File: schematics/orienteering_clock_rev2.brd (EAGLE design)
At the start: 100 x 80 mm, 53 parts, among them IC1 TPIC6B595N, IC2 TPIC6B595N, J2 ICSP, Q1 IRFU9024V, Q2 IRFU9024V, Q3 IRFU9024V, Q4 IRFU9024V, Q5 IRFU9024V, Q6 IRFU9024V, T1 BC547, Y2 16MHz

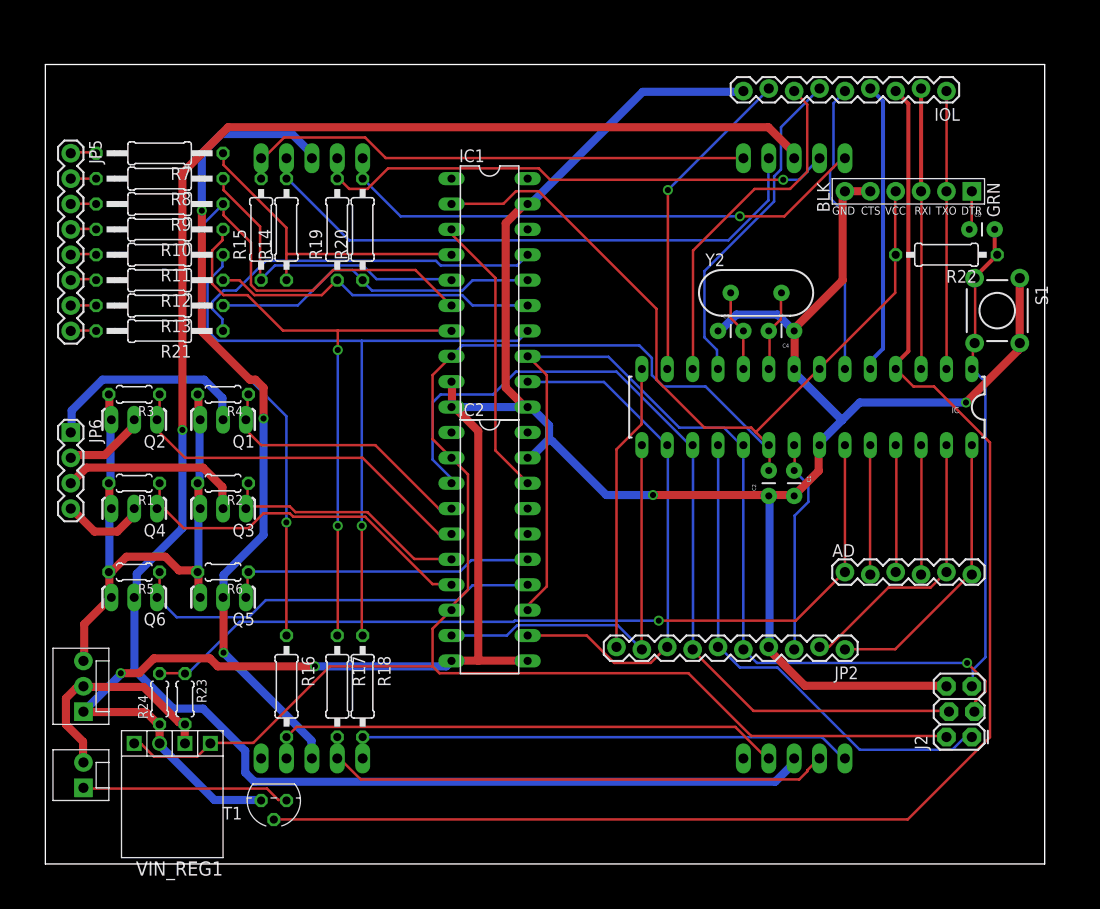
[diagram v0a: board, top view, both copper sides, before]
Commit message: schematics: improvements
- better packages for resistors
- slightly better placement
- added power_out outlet
- wider net for VCC
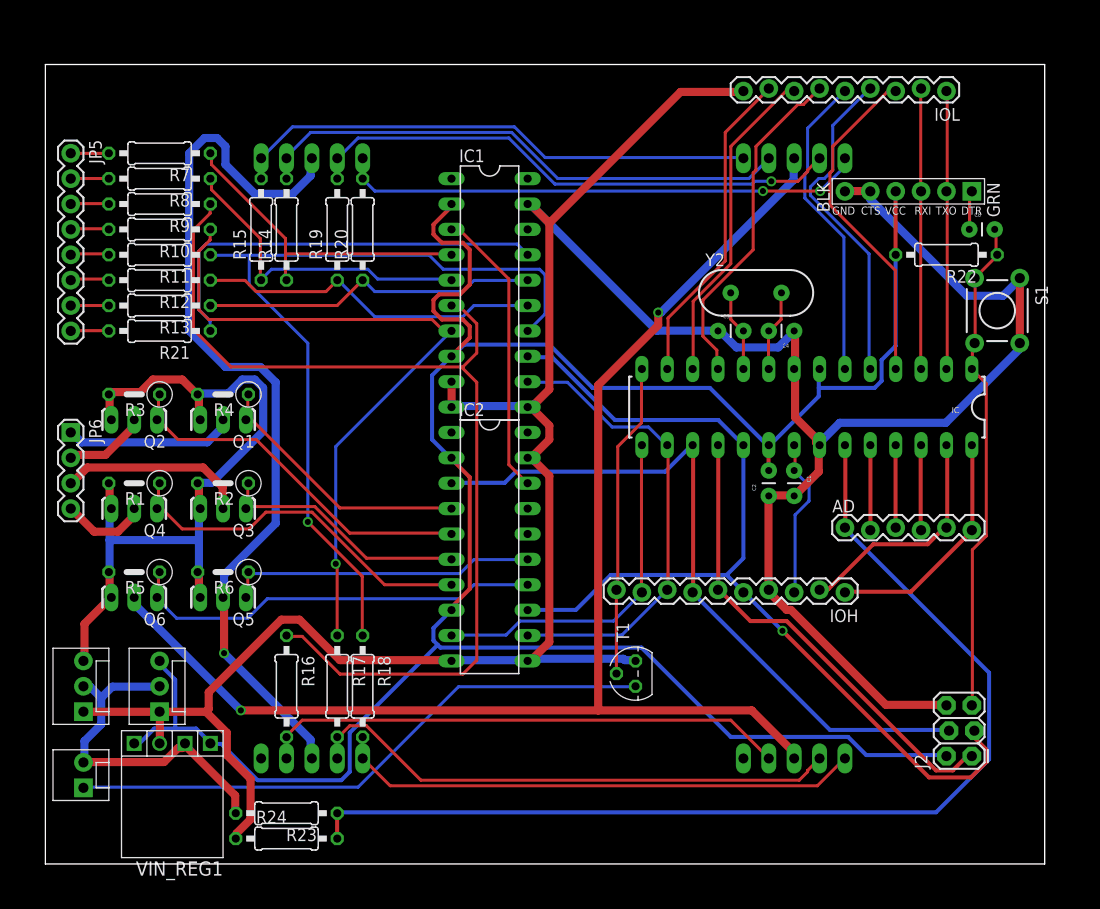
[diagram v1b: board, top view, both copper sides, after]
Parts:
- added IOH: M10LOCK, SparkFun-Connectors:1X10_LOCK
- JP2: value M10LOCK -> POWER_OUT; device SparkFun-Connectors:1X10_LOCK -> SparkFun-Connectors:MOLEX-1X3
- R1, R2, R3, R4, R5, R6: device resistor:0204/5 -> resistor:0207/5V
- R10, R11, R12, R13, R21, R7, R8, R9: device resistor:0207/12 -> resistor:0207/10
- R23, R24: device resistor:0204/5 -> resistor:0207/10
- moved JP2 68.9 mm to (11.4, 15.2), turned to 90 degrees
- moved T1 38.4 mm to (59.1, 19.1), turned to 90 degrees
- moved R24 18.9 mm to (24.1, 2.54), turned to 0 degrees
- moved R23 15.3 mm to (24.1, 5.08), turned to 180 degrees
- moved AD 4.45 mm to (80.0, 33.7)
- moved J2 1.90 mm to (92.7, 10.8)
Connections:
- net AD4/SDA: now also IOH.2; no longer JP2.2
- net AD5/SCL: now also IOH.1; no longer JP2.1
- net AREF: now also IOH.3; no longer JP2.3
- net GND: now also IOH.4, JP2.1; no longer JP2.4
- net IO2: no longer T1.2
- net IO8: now also IOH.10, T1.2; no longer JP2.10
- net IO9: now also IOH.9; no longer JP2.9
- net MISO: now also IOH.6; no longer JP2.6
- net MOSI: now also IOH.7; no longer JP2.7
- net SCK: now also IOH.5; no longer JP2.5
- net SS: now also IOH.8; no longer JP2.8
- net VCC: now also JP2.3
- net VIN: now also JP2.2
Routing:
- net IO2: track 145.9 -> 33.7 mm
- net A_S2: track 189.6 -> 136.9 mm, vias 1 -> 2
- net BUZZ_-: track 20.9 -> 59.4 mm
- net AD0: track 85.5 -> 107.5 mm, vias 1 -> 0
- net D2: track 79.3 -> 101.1 mm, vias 1 -> 0
- net DISP_12V: track 59.5 -> 76.1 mm
- net MOSI: track 88.0 -> 71.9 mm
- net VIN: track 23.0 -> 35.9 mm
- net D4: track 70.7 -> 83.4 mm
- net A_S1: track 81.9 -> 90.9 mm, vias 3 -> 1
- net D3: track 62.4 -> 70.0 mm, vias 2 -> 1
- net GND: track 301.6 -> 308.8 mm, vias 4 -> 0
- net SS: track 52.6 -> 47.0 mm
- net AREF: track 21.7 -> 16.1 mm
- net IO9: track 40.9 -> 35.7 mm
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
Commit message: schematics: redid connections to comply with various DRC
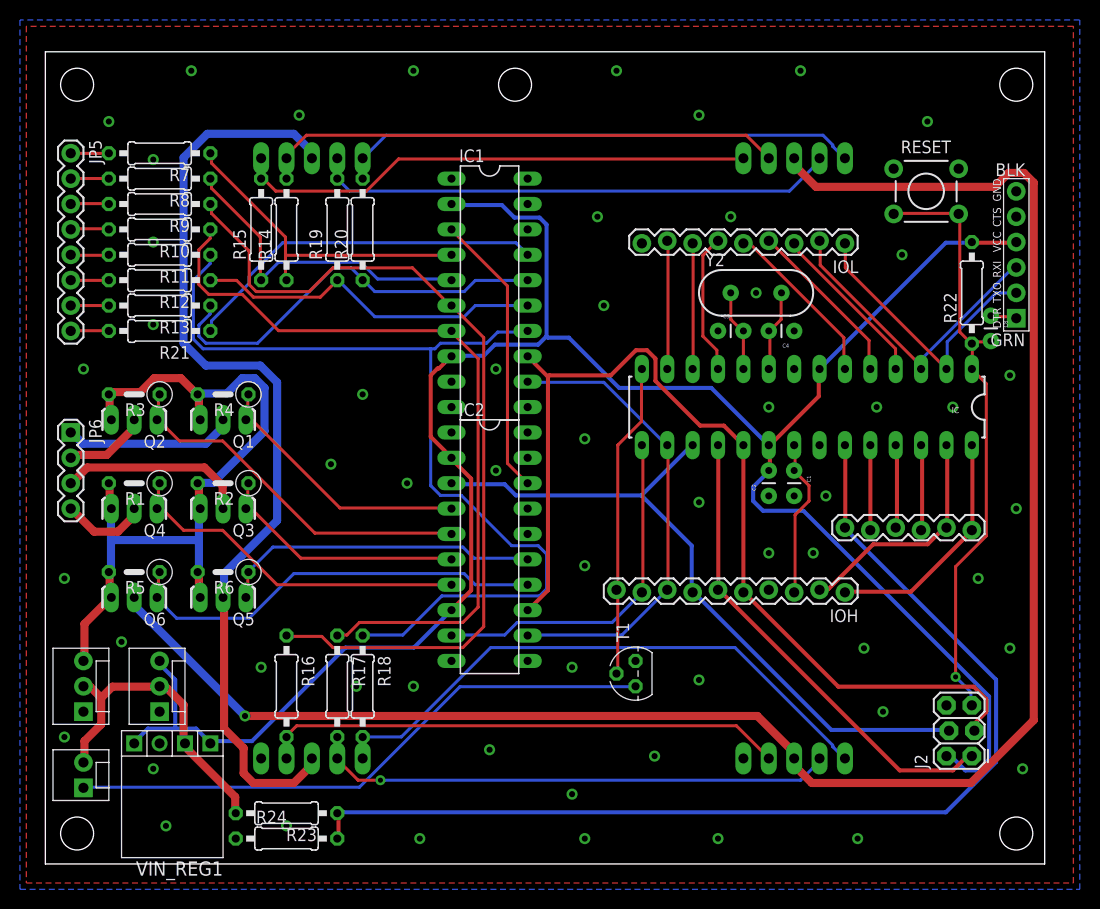
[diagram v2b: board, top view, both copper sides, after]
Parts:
- removed S1: RESET, SparkFun:TACTILE-PTH
- added JP10, JP11, JP4, JP8, JP9: STAND-OFF, SparkFun:STAND-OFF
- added RESET: RESET, SparkFun:TACTILE-PTH
- AD: value (none) -> AD
- moved IOL 18.3 mm to (80.0, 62.2)
- moved JP7 12.5 mm to (97.2, 61.0), turned to 90 degrees
- moved C8 8.90 mm to (94.6, 54.9), turned to 270 degrees
- moved R22 4.58 mm to (92.7, 57.1), turned to 90 degrees
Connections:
- net GND: now also RESET.1, RESET.2; no longer S1.1, S1.2
- net RESET: now also RESET.3, RESET.4; no longer S1.3, S1.4
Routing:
- net GND: track 308.8 -> 0.00 mm, vias 0 -> 56
- net A_S2: track 136.9 -> 181.8 mm, vias 2 -> 1
- net IO6: track 32.5 -> 12.6 mm
- net IO5: track 33.9 -> 14.1 mm
- net IO7: track 32.3 -> 12.9 mm
- net VCC: track 236.8 -> 218.2 mm
- net IO2: track 33.7 -> 16.8 mm
- net IO3: track 33.4 -> 17.1 mm
- net IO4: track 31.2 -> 17.2 mm
- net D2: track 101.1 -> 87.4 mm
- net D4: track 83.4 -> 95.7 mm, vias 1 -> 0
- net RESET: track 50.1 -> 61.0 mm, vias 0 -> 1
- net D6: track 33.7 -> 41.3 mm
- net D3: track 70.0 -> 77.2 mm, vias 1 -> 0
- net LS_E: track 52.7 -> 58.9 mm
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- added copper zone on layer 1, net GND
- added copper zone on layer 16, net GND
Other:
- board size 100 x 80 mm -> 100 x 81.3 mm

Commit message: schematics: part names smashing for silkscreen
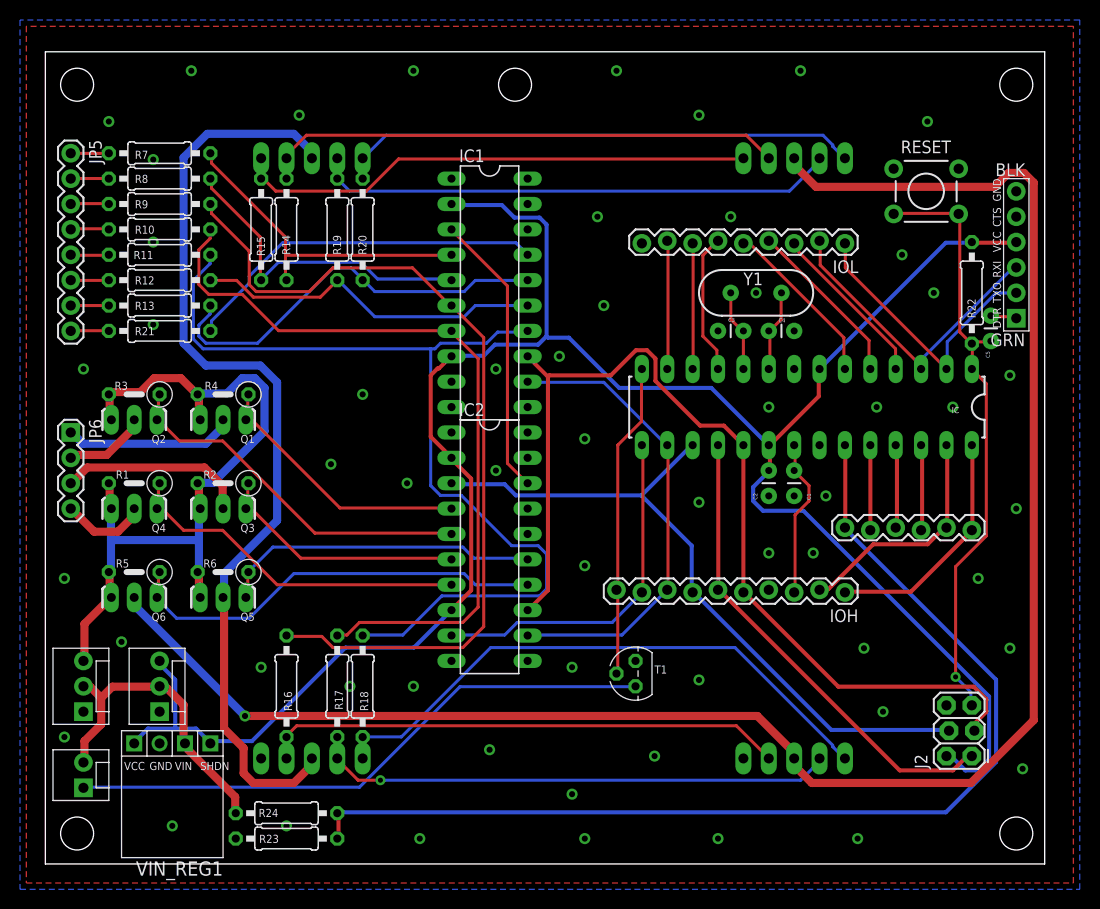
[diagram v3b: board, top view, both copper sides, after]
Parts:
- R22: value 10k -> 10K
- renumbered C8 to C5, Y2 to Y1
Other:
- board text added: "GND"
- board text added: "SHDN"
- board text added: "VCC"
- board text added: "VIN"

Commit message: schematics: modified POWER packages/schema, texts on top silkscreen
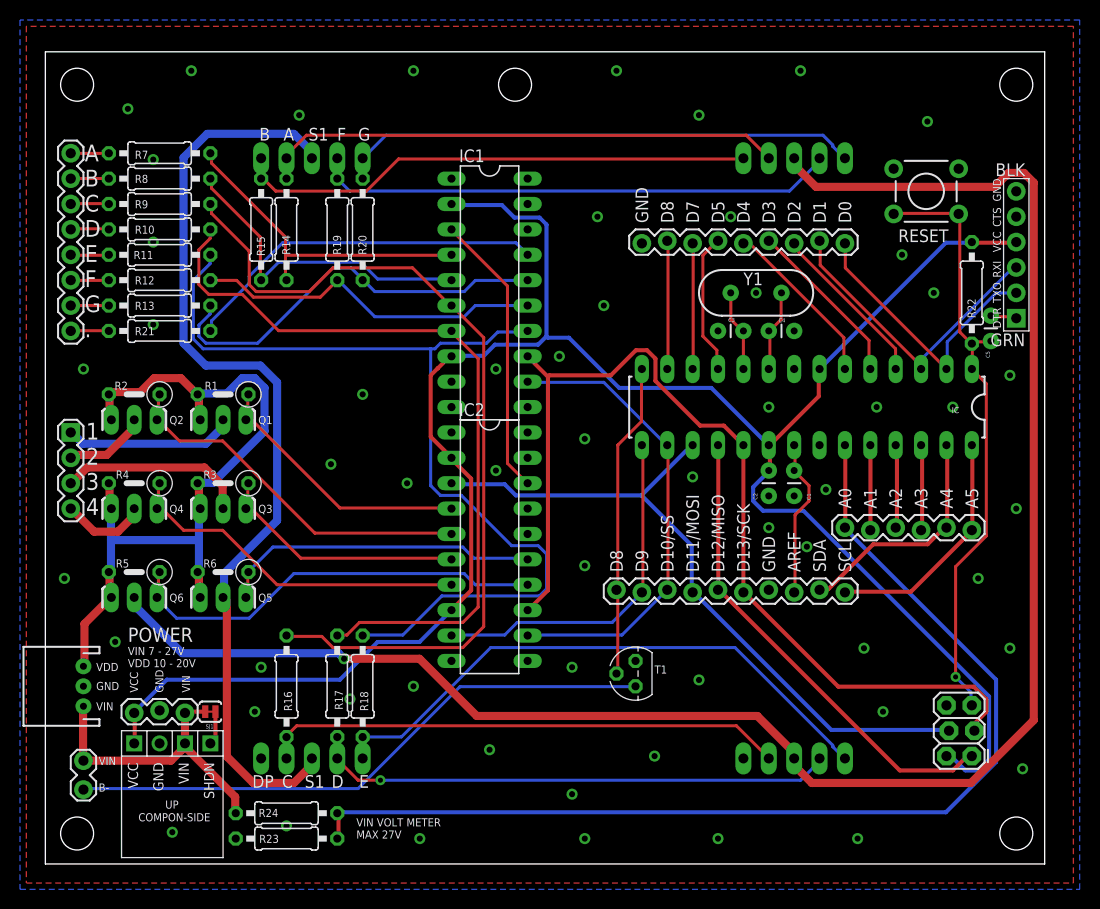
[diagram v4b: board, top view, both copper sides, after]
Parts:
- added SJ1: SHDN_PULLUP, SparkFun-Passives:PAD-JUMPER-2-NC_BY_TRACE_YES_SILK
- JP1: value POWER_IN -> DC_IN; device SparkFun-Connectors:MOLEX-1X3 -> SparkFun-Connectors:JST-3-PTH
- JP2: device SparkFun-Connectors:MOLEX-1X3 -> SparkFun-Connectors:1X03_LOCK
- JP3: device SparkFun-Connectors:MOLEX-1X2 -> SparkFun-Connectors:1X02_LOCK
- VIN_REG1: value POLOLU_D24V3F5-HC -> POLOLU_D24V3F5
- moved R1 12.6 mm to (17.8, 47.0)
- moved R2 12.6 mm to (8.89, 47.0)
- moved R3 12.6 mm to (17.8, 38.1)
- moved R4 12.6 mm to (8.89, 38.1)
- moved JP1 2.54 mm to (3.81, 17.8)
- moved JP2 2.54 mm to (14.0, 15.2), turned to 180 degrees
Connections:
- new net N$1: SJ1.2, VIN_REG1.S
- net B_1: now also R1.1; no longer R4.1
- net B_2: now also R2.1; no longer R3.1
- net B_3: now also R3.1; no longer R2.1
- net B_4: now also R4.1; no longer R1.1
- net GND: now also JP1.2, JP2.2; no longer JP1.1, JP2.1
- net VCC: no longer VIN_REG1.S
- net VIN: now also JP1.1, JP2.1, SJ1.1; no longer JP1.2, JP2.2
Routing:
- net VCC: track 218.2 -> 211.3 mm
- net N$1: track 0.00 -> 3.39 mm
- net VIN: track 31.9 -> 30.9 mm
- net DISP_12V: track 76.5 -> 77.0 mm
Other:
- board text added: "1 2 3 4"
- board text added: "A"
- board text added: "A B C D E F G ."
- board text added: "A0"
- board text added: "A1"
- board text added: "A2"
- board text added: "A3"
- board text added: "A4"
- board text added: "A5"
- board text added: "AREF"
- board text added: "B"
- board text added: "B-"
- board text added: "C"
- board text added: "D"
- board text added: "D0"
- board text added: "D1"
- board text added: "D10/SS"
- board text added: "D11/MOSI"
- board text added: "D12/MISO"
- board text added: "D13/SCK"
- board text added: "D2"
- board text added: "D3"
- board text added: "D4"
- board text added: "D5"
- board text added: "D7"
- board text added: "D8"
- board text added: "D9"
- board text added: "DP"
- board text added: "E"
- board text added: "F"
- board text added: "G"
- board text added: "POWER"
- board text added: "S1"
- board text added: "SCL"
- board text added: "SDA"
- board text added: "VDD"
- board text added: "VIN 7 - 27V VDD 10 - 20V"
- board text added: "VIN VOLT METER MAX 27V"
- board text removed: "SHDN"

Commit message: schematics: changed position of small LED segments
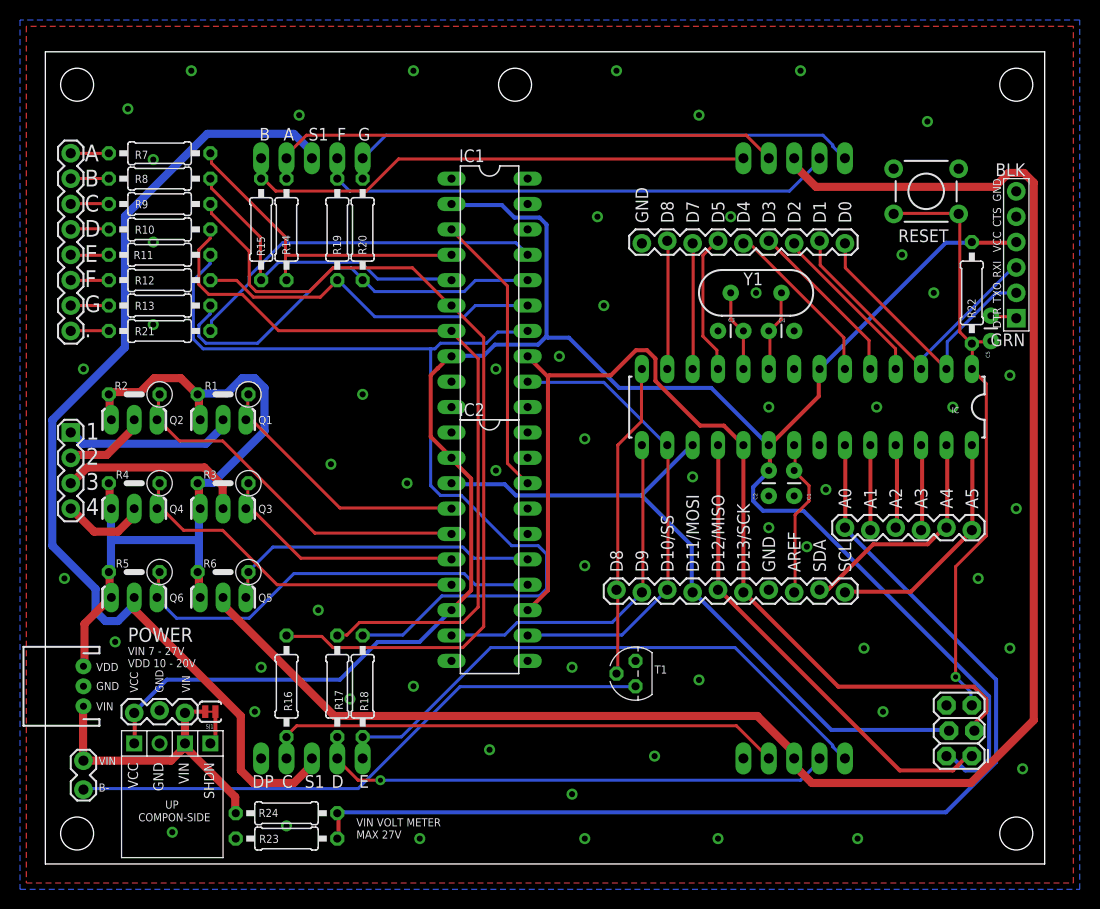
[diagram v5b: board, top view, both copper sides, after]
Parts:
- moved LED_SMALL_1 48.3 mm to (74.9, 40.6)
- moved LED_SMALL_2 48.3 mm to (26.7, 40.6)
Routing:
- net A_S2: track 181.8 -> 104.3 mm, vias 1 -> 0
- net A_S1: track 95.7 -> 172.9 mm

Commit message: schematics: added option to use LM7805 as voltage regulator
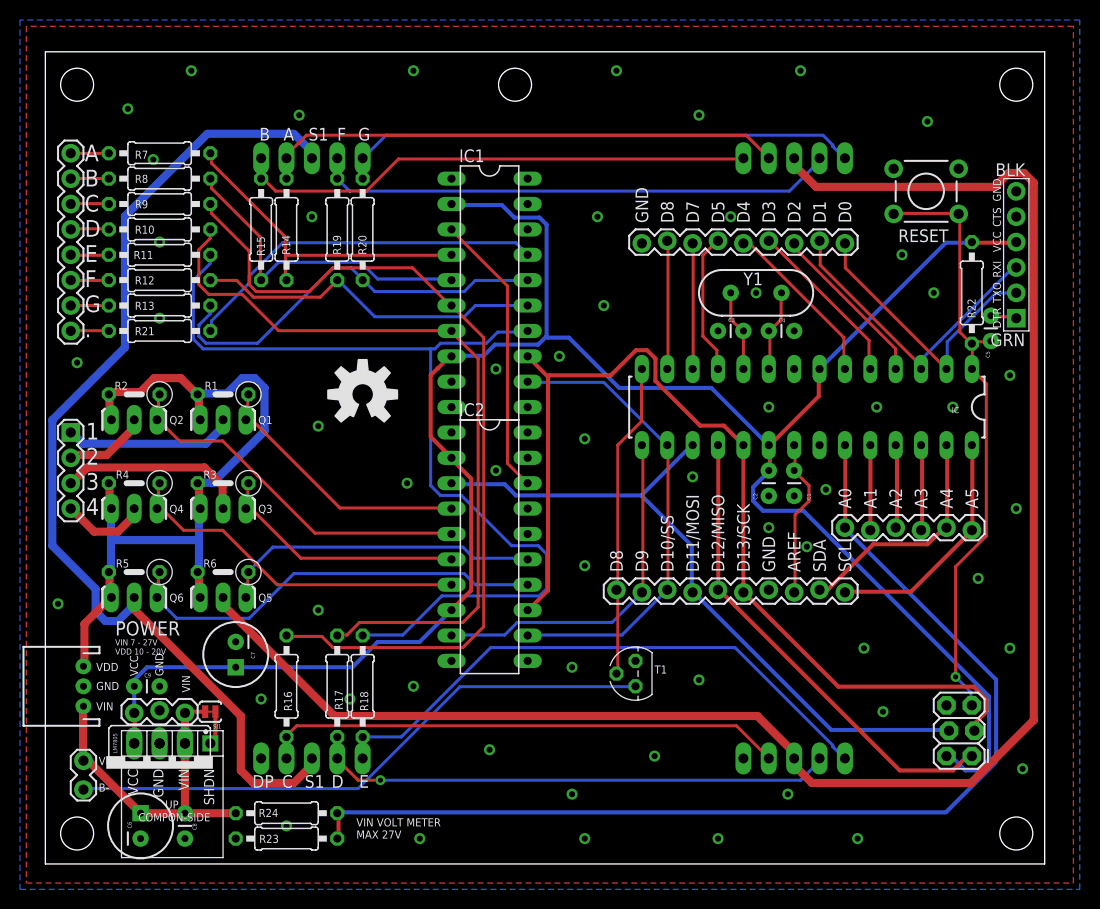
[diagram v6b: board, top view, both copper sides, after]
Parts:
- added C6, C7: 470uF, SparkFun-Passives:CPOL-RADIAL-100UF-25V
- added C8, C9: 100nF, SparkFun-Passives:CAP-PTH-SMALL
- added E$1: (no value), SparkFun-Aesthetics:OSHW-LOGO-L
- added LM7805: (no value), v-reg:78XXS
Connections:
- net GND: now also C6.2, C7.2, C8.2, C9.2, LM7805.GND
- net VCC: now also C7.1, C9.1, LM7805.OUT
- net VIN: now also C6.1, C8.1, LM7805.IN
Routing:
- net VIN: track 30.9 -> 45.2 mm
- net VCC: track 211.3 -> 213.3 mm
